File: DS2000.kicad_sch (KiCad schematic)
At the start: 55 parts, among them J1 USB-C, J3 USB wire, SW1 MUTE, SW2 DEAFEN, SW3 DISCONNECT, U1 USBLC6-2SC6, U2 XC6206P332MR, U3 RP2350A, U4 W25Q16JVSS, U5 74AHCT1G125, Y1 12MHz

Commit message: fix: back to the reference crystal, ABM8-272-T3 with 15 pF
JLC's design review flagged the basic YXC crystal against Raspberry Pi's
RP2350 hardware design guide. A crystal that does not start costs a whole
batch, against one extended-part fee: Y1 is the Abracon ABM8-272-T3 again
(C20625731, Economic PCBA) with 15 pF load caps (C1548), as the reference.

Co-Authored-By: Claude Opus 5.5 <noreply@anthropic.com>
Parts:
- C17, C18: value 33p -> 15p; LCSC C1562 -> C1548; MPN 0402CG330J500NT -> 0402CG150J500NT
- Y1: LCSC C9002 -> C20625731; MPN X322512MSB4SI -> ABM8-272-T3; Manufacturer YXC -> Abracon
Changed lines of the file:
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@@
 			)
 		)
-		(property "MPN" "X322512MSB4SI"
+		(property "MPN" "ABM8-272-T3"
 			(at 127 214.63 0)
 			(hide yes)
@@
 			)
 		)
-		(property "Manufacturer" "YXC"
+		(property "Manufacturer" "Abracon"
 			(at 127 214.63 0)
 			(hide yes)
@@
 			)
 		)
-		(property "LCSC" "C9002"
+		(property "LCSC" "C20625731"
 			(at 127 214.63 0)
 			(hide yes)
@@
 			)
 		)
-		(property "Value" "33p"
+		(property "Value" "15p"
 			(at 133.6 224.79 0)
 			(show_name no)
@@
 			)
 		)
-		(property "MPN" "0402CG330J500NT"
+		(property "MPN" "0402CG150J500NT"
 			(at 133.6 222.88 0)
 			(hide yes)
@@
 			)
 		)
-		(property "LCSC" "C1562"
+		(property "LCSC" "C1548"
 			(at 133.6 222.88 0)
 			(hide yes)
@@
 			)
 		)
-		(property "Value" "33p"
+		(property "Value" "15p"
 			(at 115.82 214.63 0)
 			(show_name no)
@@
 			)
 		)
-		(property "MPN" "0402CG330J500NT"
+		(property "MPN" "0402CG150J500NT"
 			(at 115.82 212.72 0)
 			(hide yes)
@@
 			)
 		)
-		(property "LCSC" "C1562"
+		(property "LCSC" "C1548"
 			(at 115.82 212.72 0)
 			(hide yes)

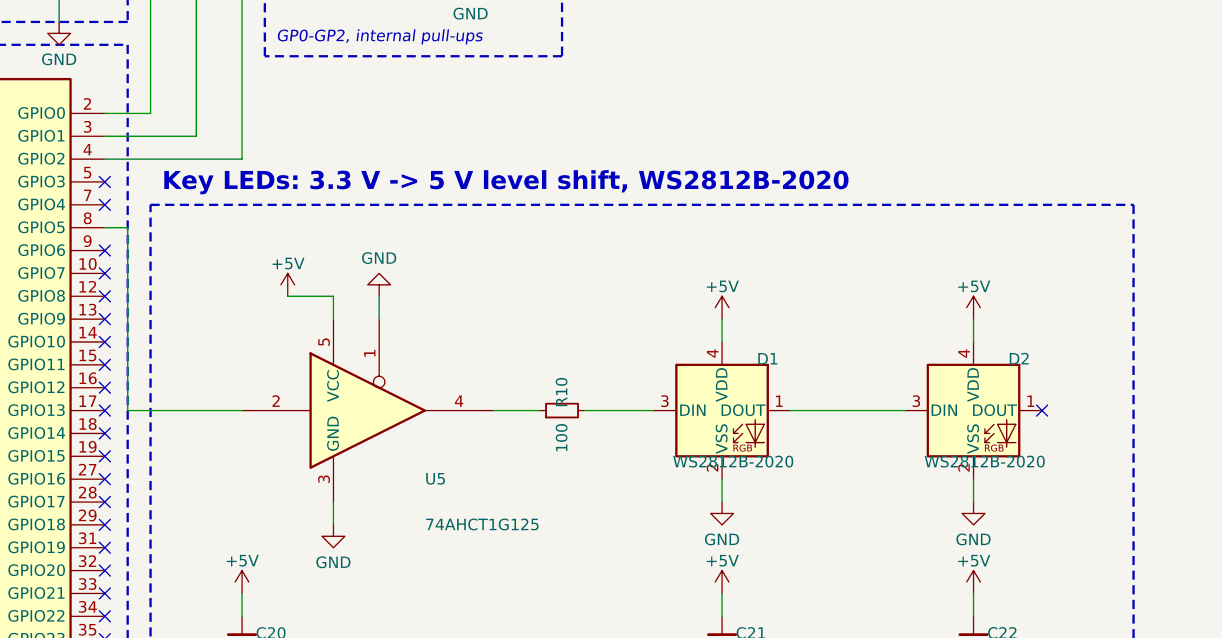
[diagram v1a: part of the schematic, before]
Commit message: fix: SK6805-EC20 key LEDs, which JLC assembles in Economic PCBA
JLC's order review reported the WS2812B-2020 (C52917434) as Standard-PCBA
only, which brings back the setup fee and a 70 mm minimum board side. The
OPSCO SK6805-EC20 (C2890036) is the same 2.0 x 2.0 mm top-emitting,
WS2812-compatible part (800 kHz, GRB), assembles in Economic, and is
thinner: 0.65 mm instead of 0.84, more room under the Choc V1 housing.

- Its pinout (1 VDD, 2 DOUT, 3 GND, 4 DIN) is not in KiCad's library, so
  the project gets its own symbol library (DS2000.kicad_sym, sym-lib-table)
  and footprint (datasheet land pattern: 0.8 x 0.7 mm pads), plus a STEP
  model from gen_models.py.
- Turned 270 deg, every net keeps its corner: the routing only follows the
  pads, and the +5V run under D2 moves 0.2 mm down to clear the longer pads.
- DIN needs 0.7 x VDD, so U5's level shifter is now required.
- 5 mA per colour, about half a WS2812B: to confirm through a keycap.

ERC 0. DRC: 0 unconnected, 0 parity issues; the known 15 notes only.

Co-Authored-By: Claude Opus 5.5 <noreply@anthropic.com>
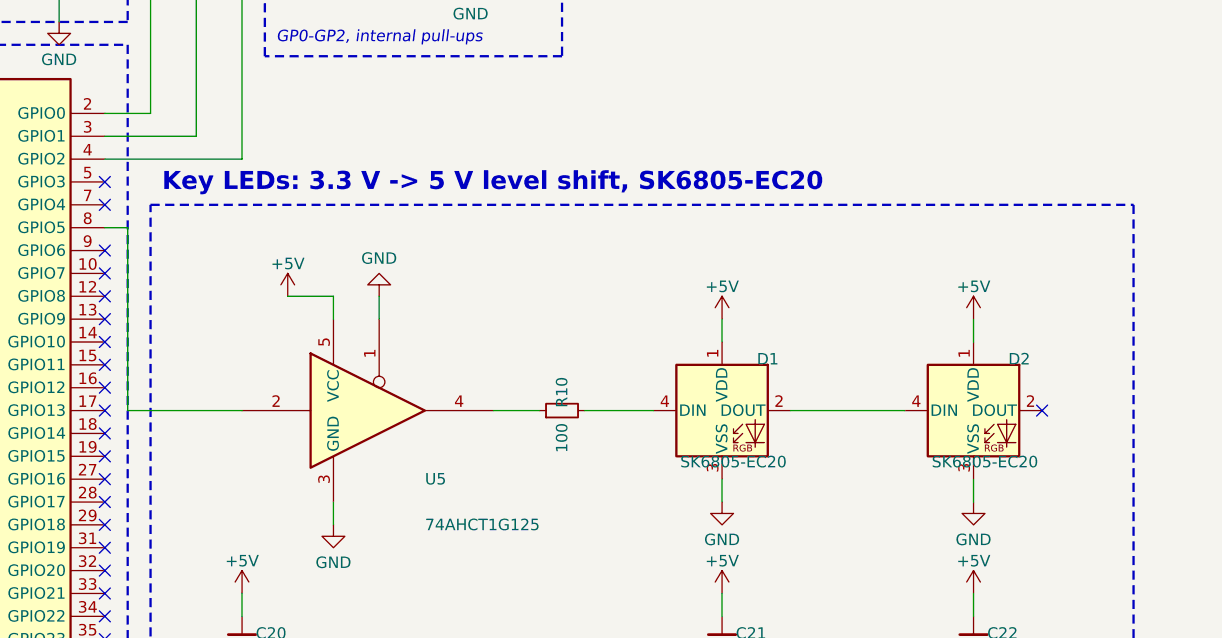
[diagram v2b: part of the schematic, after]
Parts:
- D1, D2: value WS2812B-2020 -> SK6805-EC20; footprint LED_SMD:LED_WS2812B-2020_PLCC4_2.0x2.0mm -> DS2000:LED_SK6805-EC20_2.0x2.0mm; symbol LED:WS2812B-2020 -> DS2000:SK6805-EC20; LCSC C52917434 -> C2890036; MPN WS2812B-2020-V6 -> SK6805-EC20; Manufacturer Worldsemi -> OPSCO Optoelectronics
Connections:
- net +5V: now also D1.1 (VDD), D2.1 (VDD); no longer D1.4 (VDD), D2.4 (VDD)
- net GND: now also D1.3 (VSS), D2.3 (VSS); no longer D1.2 (VSS), D2.2 (VSS)
- net at R10.2: now also D1.4 (DIN); no longer D1.3 (DIN)
- new net: D1.2 (DOUT), D2.4 (DIN)
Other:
- note added: "Key LEDs: 3.3 V -> 5 V level shift, SK6805-EC20"
- note removed: "Key LEDs: 3.3 V -> 5 V level shift, WS2812B-2020"
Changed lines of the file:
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@@
 		)
 	)
-	(text "Key LEDs: 3.3 V -> 5 V level shift, WS2812B-2020"
+	(text "Key LEDs: 3.3 V -> 5 V level shift, SK6805-EC20"
 		(exclude_from_sim no)
 		(at 214.63 166.37 0)
@@
 	)
 	(symbol
-		(lib_id "LED:WS2812B-2020")
+		(lib_id "DS2000:SK6805-EC20")
 		(at 304.8 190.5 0)
 		(unit 1)
@@
 			)
 		)
-		(property "Value" "WS2812B-2020"
+		(property "Value" "SK6805-EC20"
 			(at 306.07 196.215 0)
 			(show_name no)
@@
 			)
 		)
-		(property "Footprint" "LED_SMD:LED_WS2812B-2020_PLCC4_2.0x2.0mm"
+		(property "Footprint" "DS2000:LED_SK6805-EC20_2.0x2.0mm"
 			(at 304.8 190.5 0)
 			(hide yes)
@@
 			)
 		)
-		(property "MPN" "WS2812B-2020-V6"
+		(property "MPN" "SK6805-EC20"
 			(at 309.88 184.785 0)
 			(hide yes)
@@
 			)
 		)
-		(property "Manufacturer" "Worldsemi"
+		(property "Manufacturer" "OPSCO Optoelectronics"
 			(at 309.88 184.785 0)
 			(hide yes)
@@
 			)
 		)
-		(property "LCSC" "C52917434"
+		(property "LCSC" "C2890036"
 			(at 309.88 184.785 0)
 			(hide yes)
@@
 	)
 	(symbol
-		(lib_id "LED:WS2812B-2020")
+		(lib_id "DS2000:SK6805-EC20")
 		(at 276.86 190.5 0)
 		(unit 1)
@@
 			)
 		)
-		(property "Value" "WS2812B-2020"
+		(property "Value" "SK6805-EC20"
 			(at 278.13 196.215 0)
 			(show_name no)
@@
 			)
 		)
-		(property "Footprint" "LED_SMD:LED_WS2812B-2020_PLCC4_2.0x2.0mm"
+		(property "Footprint" "DS2000:LED_SK6805-EC20_2.0x2.0mm"
 			(at 276.86 190.5 0)
 			(hide yes)
@@
 			)
 		)
-		(property "MPN" "WS2812B-2020-V6"
+		(property "MPN" "SK6805-EC20"
 			(at 281.94 184.785 0)
 			(hide yes)
@@
 			)
 		)
-		(property "Manufacturer" "Worldsemi"
+		(property "Manufacturer" "OPSCO Optoelectronics"
 			(at 281.94 184.785 0)
 			(hide yes)
@@
 			)
 		)
-		(property "LCSC" "C52917434"
+		(property "LCSC" "C2890036"
 			(at 281.94 184.785 0)
 			(hide yes)

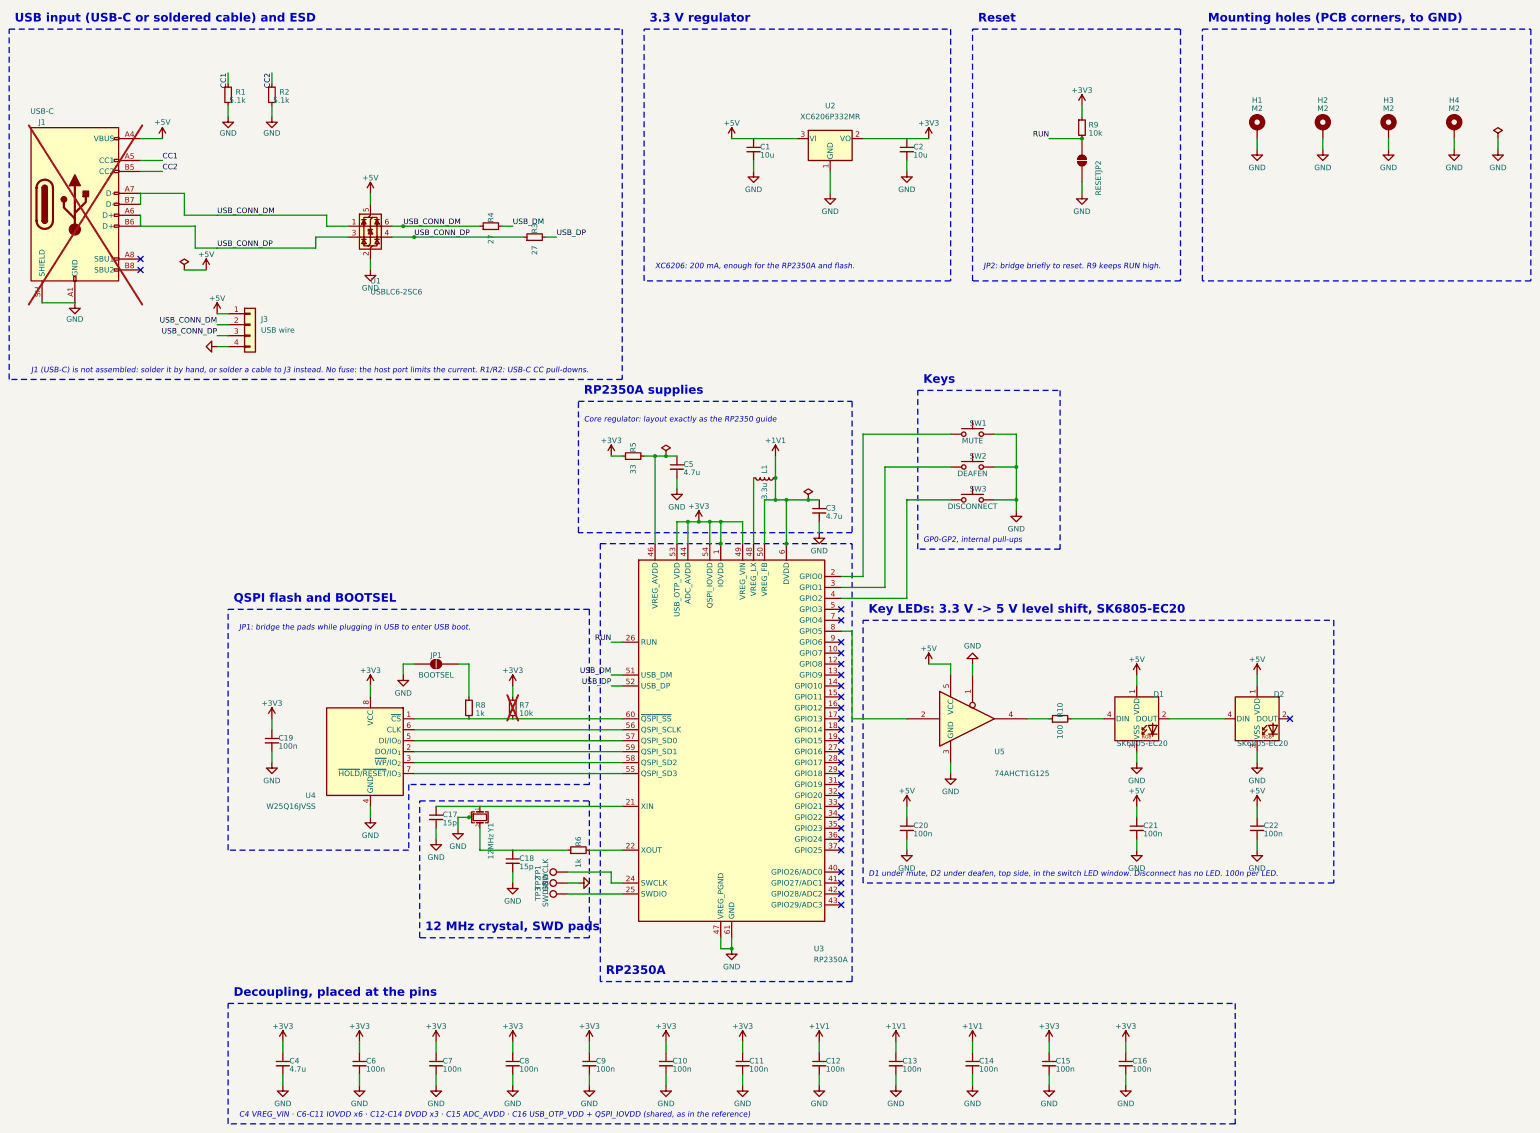
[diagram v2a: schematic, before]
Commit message: feat: production review changes to the board and schematic
- U4: 4 MB flash (W25Q32JVSSIQ, C82344), the RP2350-Zero's size, room for
  A/B firmware updates
- C1/C2: 10u -> 4.7u (CL21A475KAQNNNE, C1779, basic), so VBUS stays near
  USB 2.0's 10 uF
- J1 is no longer DNP: a `Config` field (+standard) lets the KiBot variant
  decide whether JLC fits it (standard) or it is soldered by hand (economic)
- J3: four SMD wire pads on the bottom beside J1 (WirePads_1x04_P2.54mm_SMD)
  instead of through holes on the visible face; its USB branch drops from
  ~20 mm to ~12 mm per line
- USB pair from J3 to U1 hand-routed as a coupled pair, 0.25 mm / 0.15 mm
  (~90 ohm on JLC04161H-7628); USB net class updated to match
- R1 moves below the pair, CC1 via moved with it
- BOOTSEL (R8 -> JP1): 95 mm -> 53 mm, three vias, kept clear of J1's shell
- TP4-TP6: production test pads for +5V, +3V3 and +1V1 on the bottom, new
  stage in the schematic
- F.Cu GND pour restored (lost in 56300c4); both logos' exposed copper is
  now a GND pad, so it no longer floats on the touchable face
- JLCJLCJLCJLC on B.SilkS, so JLC's order number goes underneath
- title blocks: DS2000, 2026-10-23, current LEDs

ERC 0; DRC 0 errors, 0 unconnected, schematic parity clean (known warnings:
TrueType text thickness, J1/Y1 footprints edited on the board).

Co-Authored-By: Claude Opus 5.5 <noreply@anthropic.com>
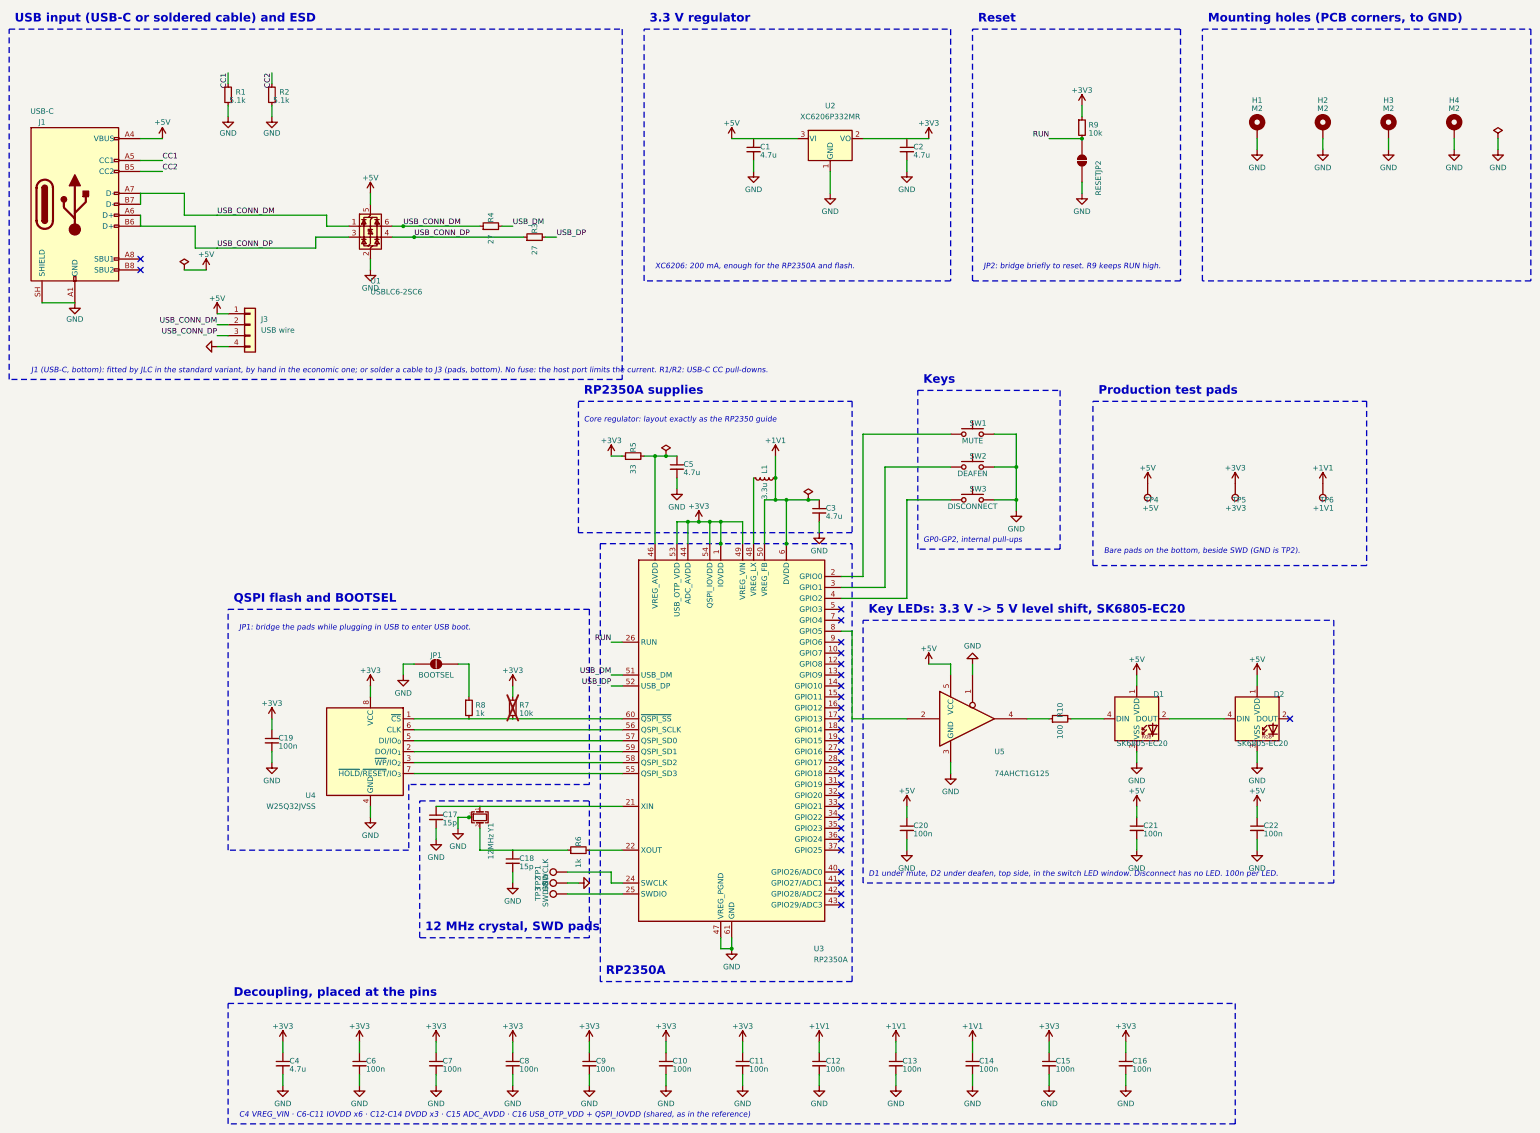
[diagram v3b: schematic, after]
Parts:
- added TP4: +5V, TestPoint:TestPoint_Pad_D1.5mm, symbol Connector:TestPoint
- added TP5: +3V3, TestPoint:TestPoint_Pad_D1.5mm, symbol Connector:TestPoint
- added TP6: +1V1, TestPoint:TestPoint_Pad_D1.5mm, symbol Connector:TestPoint
- C1, C2: value 10u -> 4.7u; LCSC C15850 -> C1779; MPN CL21A106KAYNNNE -> CL21A475KAQNNNE
- J1: Config (none) -> +standard; now fitted; now in the parts list
- J3: footprint Connector_PinHeader_2.54mm:PinHeader_1x04_P2.54mm_Vertical -> DS2000:WirePads_1x04_P2.54mm_SMD
- U4: value W25Q16JVSS -> W25Q32JVSS; LCSC C82317 -> C82344; MPN W25Q16JVSSIQ -> W25Q32JVSSIQ
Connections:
- net +1V1: now also TP6.1
- net +3V3: now also TP5.1
- net +5V: now also TP4.1
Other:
- note added: "Bare pads on the bottom, beside SWD (GND is TP2)."
- note added: "J1 (USB-C, bottom): fitted by JLC in the standard variant, by hand in the economic one; or solder a cable to J3 (pads, bottom). No fuse: the host port limits the current. R1/R2: USB-C CC pull-downs."
- note added: "Production test pads"
- note removed: "J1 (USB-C) is not assembled: solder it by hand, or solder a cable to J3 instead. No fuse: the host port limits the current. R1/R2: USB-C CC pull-downs."
- title: DS-2000 -> DS2000

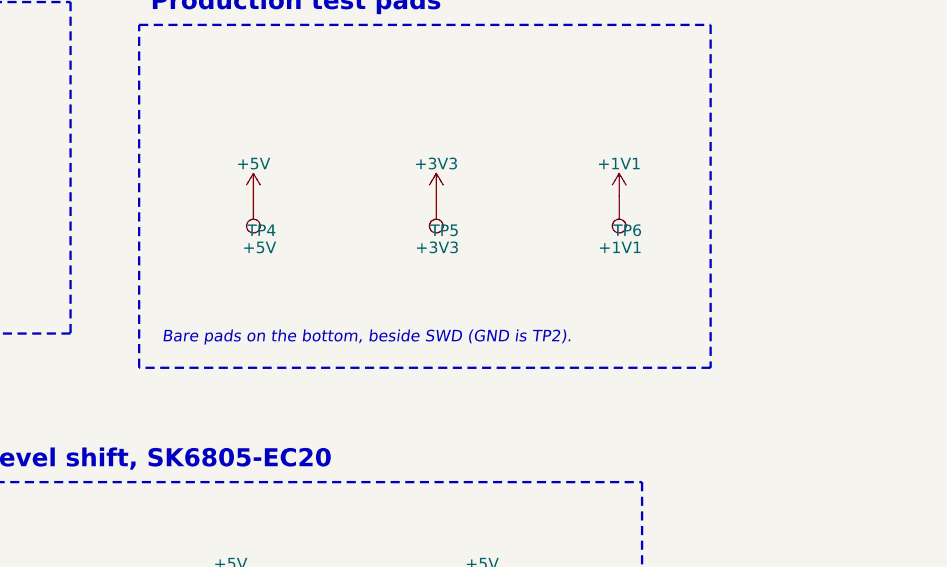
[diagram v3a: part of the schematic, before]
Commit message: fix: keep the test pads' labels clear of their symbols, correct the stage note
Co-Authored-By: Claude Opus 5.5 <noreply@anthropic.com>
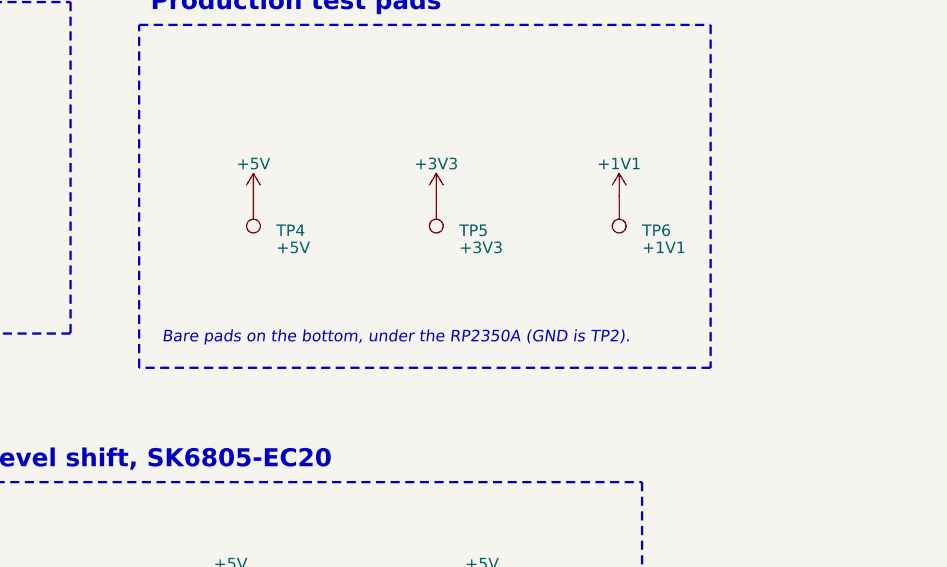
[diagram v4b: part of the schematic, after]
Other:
- note added: "Bare pads on the bottom, under the RP2350A (GND is TP2)."
- note removed: "Bare pads on the bottom, beside SWD (GND is TP2)."
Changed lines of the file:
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@@
 					(size 1.27 1.27)
 				)
-				(justify left)
+				(justify right)
 			)
 		)
@@
 					(size 1.27 1.27)
 				)
-				(justify left)
+				(justify right)
 			)
 		)
@@
 					(size 1.27 1.27)
 				)
-				(justify left)
+				(justify right)
 			)
 		)
@@
 					(size 1.27 1.27)
 				)
-				(justify left)
+				(justify right)
 			)
 		)
@@
 					(size 1.27 1.27)
 				)
-				(justify left)
+				(justify right)
 			)
 		)
@@
 					(size 1.27 1.27)
 				)
-				(justify left)
+				(justify right)
 			)
 		)
@@
 		)
 	)
-	(text "Bare pads on the bottom, beside SWD (GND is TP2)."
+	(text "Bare pads on the bottom, under the RP2350A (GND is TP2)."
 		(exclude_from_sim no)
 		(at 269.24 152.4 0)

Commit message: feat: hybrid Choc V1 / MX switch footprint for prototypes
SW1-SW3 take either a Kailh Choc V1 (product) or a 3-pin MX (prototypes):
MX pins added, shared 4 mm centre hole, tracks moved off the new pins.

Co-Authored-By: Claude Opus 5.5 <noreply@anthropic.com>
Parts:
- SW1, SW2, SW3: footprint DS2000:SW_Kailh_Choc_V1_1.00u -> DS2000:SW_Hybrid_Choc_V1_MX_1.00u
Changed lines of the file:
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@@
 			)
 		)
-		(property "Footprint" "DS2000:SW_Kailh_Choc_V1_1.00u"
+		(property "Footprint" "DS2000:SW_Hybrid_Choc_V1_MX_1.00u"
 			(at 238.76 139.7 0)
 			(hide yes)
@@
 			)
 		)
-		(property "Footprint" "DS2000:SW_Kailh_Choc_V1_1.00u"
+		(property "Footprint" "DS2000:SW_Hybrid_Choc_V1_MX_1.00u"
 			(at 238.76 132.08 0)
 			(hide yes)
@@
 			)
 		)
-		(property "Footprint" "DS2000:SW_Kailh_Choc_V1_1.00u"
+		(property "Footprint" "DS2000:SW_Hybrid_Choc_V1_MX_1.00u"
 			(at 238.76 124.46 0)
 			(hide yes)
